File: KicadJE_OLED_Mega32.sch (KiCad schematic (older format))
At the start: 86 parts, among them J205 OUT1, J206 OUT2, J207 IN1, J208 IN2, J209 CV1, J210 CV2, SW201 Rotary_Encoder_Switch, SW202 Rotary_Encoder_Switch, U201 TL072

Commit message: Most components placed
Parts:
- removed C216, C217: 100n, AJ:C_0805_AJ, symbol Device:C
- gave numbers to parts that had none: 12
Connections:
- net 27_A3: no longer C219.1, R234.1
- net 28_A4: no longer C212.1, R230.2, SW202.A
- net 29_A5: no longer C210.1, R226.1, SW202.B
- new net 10_INT0: C212.1, R230.2, SW202.A
- new net 11_INT1: C210.1, R226.1, SW202.B
- new net D1: C219.1, R234.1
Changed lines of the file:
@@
 $EndDescr
 $Comp
-L Eurorack:Doepfer_Power_16pin P?
+L Eurorack:Doepfer_Power_16pin P201
 U 1 1 5CCBA3BD
 P 8650 1275
-F 0 "P?" H 9200 775 50  0000 C CNN
+F 0 "P201" H 9200 775 50  0000 C CNN
 F 1 "Doepfer_Power_16pin" H 8775 1825 50  0000 C CNN
 F 2 "Connector_IDC:IDC-Header_2x08_P2.54mm_Vertical" H 8650 1275 50  0001 C CNN
@@
 $EndComp
 $Comp
-L power:-12V #PWR?
+L power:-12V #PWR0112
 U 1 1 5CCD339B
 P 9350 1575
-F 0 "#PWR?" H 9350 1675 50  0001 C CNN
+F 0 "#PWR0112" H 9350 1675 50  0001 C CNN
 F 1 "-12V" V 9365 1703 50  0000 L CNN
 F 2 "" H 9350 1575 50  0001 C CNN
@@
 29_A5
 $Comp
-L power:+5V #PWR?
+L power:+5V #PWR0113
 U 1 1 6095FB46
 P 9975 875
-F 0 "#PWR?" H 9975 725 50  0001 C CNN
+F 0 "#PWR0113" H 9975 725 50  0001 C CNN
 F 1 "+5V" H 9990 1048 50  0000 C CNN
 F 2 "" H 9975 875 50  0001 C CNN
@@
 $EndComp
 $Comp
-L power:GND #PWR?
+L power:GND #PWR0114
 U 1 1 60960991
 P 9150 1375
-F 0 "#PWR?" H 9150 1125 50  0001 C CNN
+F 0 "#PWR0114" H 9150 1125 50  0001 C CNN
 F 1 "GND" H 9225 1375 50  0000 C CNN
 F 2 "" H 9150 1375 50  0001 C CNN
@@
 $EndComp
 $Comp
-L power:GND #PWR?
+L power:GND #PWR0115
 U 1 1 60960F4E
 P 8150 1375
-F 0 "#PWR?" H 8150 1125 50  0001 C CNN
+F 0 "#PWR0115" H 8150 1125 50  0001 C CNN
 F 1 "GND" H 8155 1202 50  0000 C CNN
 F 2 "" H 8150 1375 50  0001 C CNN
@@
 	9000 1175 9050 1175
 $Comp
-L power:+5V #PWR?
+L power:+5V #PWR0116
 U 1 1 6097BBB3
 P 3650 4250
-F 0 "#PWR?" H 3650 4100 50  0001 C CNN
+F 0 "#PWR0116" H 3650 4100 50  0001 C CNN
 F 1 "+5V" H 3665 4423 50  0000 C CNN
 F 2 "" H 3650 4250 50  0001 C CNN
@@
 $EndComp
 $Comp
-L power:+5V #PWR?
+L power:+5V #PWR0117
 U 1 1 6097C13F
 P 3650 5150
-F 0 "#PWR?" H 3650 5000 50  0001 C CNN
+F 0 "#PWR0117" H 3650 5000 50  0001 C CNN
 F 1 "+5V" H 3665 5323 50  0000 C CNN
 F 2 "" H 3650 5150 50  0001 C CNN
@@
 $EndComp
 $Comp
-L power:+5V #PWR?
+L power:+5V #PWR0118
 U 1 1 6097C5E9
 P 3650 6075
-F 0 "#PWR?" H 3650 5925 50  0001 C CNN
+F 0 "#PWR0118" H 3650 5925 50  0001 C CNN
 F 1 "+5V" H 3665 6248 50  0000 C CNN
 F 2 "" H 3650 6075 50  0001 C CNN
@@
 $EndComp
 $Comp
-L power:+5V #PWR?
+L power:+5V #PWR0119
 U 1 1 6097CB1B
 P 3650 6950
-F 0 "#PWR?" H 3650 6800 50  0001 C CNN
+F 0 "#PWR0119" H 3650 6800 50  0001 C CNN
 F 1 "+5V" H 3665 7123 50  0000 C CNN
 F 2 "" H 3650 6950 50  0001 C CNN
@@
 Wire Wire Line
 	2425 1100 2350 1100
-$Comp
-L Device:C C?
-U 1 1 60ACB69E
-P 10375 1025
-AR Path="/60ACB69E" Ref="C?"  Part="1"
-AR Path="/5CD3F059/60ACB69E" Ref="C?"  Part="1"
-AR Path="/608CA457/5CD3F059/60ACB69E" Ref="C?"  Part="1"
-AR Path="/608CA457/60ACB69E" Ref="C217"  Part="1"
-F 0 "C217" H 10250 1150 50  0000 L CNN
-F 1 "100n" H 10275 950 50  0000 L CNN
-F 2 "AJ:C_0805_AJ" H 10413 875 50  0001 C CNN
-F 3 "~" H 10375 1025 50  0001 C CNN
-	1    10375 1025
-	-1   0    0    1
-$EndComp
 $Comp
 L Device:C C?
@@
 $Comp
 L Device:C C?
-U 1 1 60ACB6AB
-P 10300 1650
-AR Path="/60ACB6AB" Ref="C?"  Part="1"
-AR Path="/5CD3F059/60ACB6AB" Ref="C?"  Part="1"
-AR Path="/608CA457/5CD3F059/60ACB6AB" Ref="C?"  Part="1"
-AR Path="/608CA457/60ACB6AB" Ref="C216"  Part="1"
-F 0 "C216" H 10175 1775 50  0000 L CNN
-F 1 "100n" H 10200 1575 50  0000 L CNN
-F 2 "AJ:C_0805_AJ" H 10338 1500 50  0001 C CNN
-F 3 "~" H 10300 1650 50  0001 C CNN
-	1    10300 1650
-	-1   0    0    1
-$EndComp
-$Comp
-L Device:C C?
 U 1 1 60ACB6B1
 P 10075 1650
@@
 	1    0    0    -1
 $EndComp
-Connection ~ 10300 1500
 $Comp
 L power:GND #PWR0240
@@
 $EndComp
 $Comp
-L Device:LED D?
+L Device:LED D209
 U 1 1 60B00B05
 P 9925 1800
-F 0 "D?" H 9900 1700 50  0000 C CNN
+F 0 "D209" H 9900 1700 50  0000 C CNN
 F 1 "LED" H 9800 1900 50  0000 C CNN
 F 2 "AJ:D_0805_AJ" H 9925 1800 50  0001 C CNN
@@
 	9775 1500 9775 1800
 $Comp
-L power:+5V #PWR?
+L power:+5V #PWR0120
 U 1 1 60B1856E
 P 4675 3025
-F 0 "#PWR?" H 4675 2875 50  0001 C CNN
+F 0 "#PWR0120" H 4675 2875 50  0001 C CNN
 F 1 "+5V" H 4690 3198 50  0000 C CNN
 F 2 "" H 4675 3025 50  0001 C CNN
@@
 	10150 875  10375 875
 $Comp
-L power:+12V #PWR?
+L power:+12V #PWR0121
 U 1 1 60B94BD0
 P 10375 875
-F 0 "#PWR?" H 10375 725 50  0001 C CNN
+F 0 "#PWR0121" H 10375 725 50  0001 C CNN
 F 1 "+12V" H 10390 1048 50  0000 C CNN
 F 2 "" H 10375 875 50  0001 C CNN
@@
 	1    0    0    -1
 $EndComp
-Connection ~ 10375 875
-$Comp
-L power:+12V #PWR?
+$Comp
+L power:+12V #PWR0122
 U 1 1 60B95768
 P 9525 1175
-F 0 "#PWR?" H 9525 1025 50  0001 C CNN
+F 0 "#PWR0122" H 9525 1025 50  0001 C CNN
 F 1 "+12V" H 9540 1348 50  0000 C CNN
 F 2 "" H 9525 1175 50  0001 C CNN
@@
 $EndComp
 $Comp
-L power:+5V #PWR?
+L power:+5V #PWR0123
 U 1 1 60B96020
 P 9425 1075
-F 0 "#PWR?" H 9425 925 50  0001 C CNN
+F 0 "#PWR0123" H 9425 925 50  0001 C CNN
 F 1 "+5V" H 9440 1248 50  0000 C CNN
 F 2 "" H 9425 1075 50  0001 C CNN
@@
 Connection ~ 9050 1175
 $Comp
-L power:GND #PWR?
+L power:GND #PWR0124
 U 1 1 60BE9216
 P 4550 3275
-F 0 "#PWR?" H 4550 3025 50  0001 C CNN
+F 0 "#PWR0124" H 4550 3025 50  0001 C CNN
 F 1 "GND" H 4555 3102 50  0000 C CNN
 F 2 "" H 4550 3275 50  0001 C CNN
@@
 	4425 3275 4550 3275
 $Comp
-L Connector:Conn_01x04_Female J?
+L Connector:Conn_01x04_Female J201
 U 1 1 60BF44F5
 P 975 2100
-F 0 "J?" H 867 1675 50  0000 C CNN
+F 0 "J201" H 867 1675 50  0000 C CNN
 F 1 "OLED" H 867 1766 50  0000 C CNN
 F 2 "Connector_PinSocket_2.54mm:PinSocket_1x04_P2.54mm_Vertical" H 975 2100 50  0001 C CNN
@@
 $EndComp
 $Comp
-L power:+5V #PWR?
+L power:+5V #PWR0125
 U 1 1 60C0BC24
 P 1725 1750
-F 0 "#PWR?" H 1725 1600 50  0001 C CNN
+F 0 "#PWR0125" H 1725 1600 50  0001 C CNN
 F 1 "+5V" H 1740 1923 50  0000 C CNN
 F 2 "" H 1725 1750 50  0001 C CNN
@@
 $EndComp
 $Comp
-L Device:Jumper_NC_Dual JP?
+L Device:Jumper_NC_Dual JP201
 U 1 1 60CA048D
 P 1275 2200
-F 0 "JP?" V 1575 2125 50  0000 L CNN
+F 0 "JP201" V 1575 2125 50  0000 L CNN
 F 1 "1" H 1320 2302 50  0000 L CNN
 F 2 "Jumper:SolderJumper-3_P1.3mm_Bridged12_Pad1.0x1.5mm_NumberLabels" H 1275 2200 50  0001 C CNN
@@
 	1175 2100 1425 2100
 $Comp
-L Device:Jumper_NC_Dual JP?
+L Device:Jumper_NC_Dual JP202
 U 1 1 60CD1C03
 P 1525 2100
-F 0 "JP?" V 1925 2050 50  0000 L CNN
+F 0 "JP202" V 1925 2050 50  0000 L CNN
 F 1 "2" H 1570 2202 50  0000 L CNN
 F 2 "Jumper:SolderJumper-3_P1.3mm_Bridged12_Pad1.0x1.5mm_NumberLabels" H 1525 2100 50  0001 C CNN
@@
 $EndComp
 $Comp
-L Device:Jumper_NC_Dual JP?
+L Device:Jumper_NC_Dual JP203
 U 1 1 60CD20EB
 P 1725 2000
-F 0 "JP?" V 2075 1925 50  0000 L CNN
+F 0 "JP203" V 2075 1925 50  0000 L CNN
 F 1 "3" V 1770 2102 50  0000 L CNN
 F 2 "Jumper:SolderJumper-3_P1.3mm_Bridged12_Pad1.0x1.5mm_NumberLabels" H 1725 2000 50  0001 C CNN
@@
 	1175 1900 1800 1900
 $Comp
-L Device:Jumper_NC_Dual JP?
+L Device:Jumper_NC_Dual JP204
 U 1 1 60CD252A
 P 1900 1900
-F 0 "JP?" V 2300 1850 50  0000 L CNN
+F 0 "JP204" V 2300 1850 50  0000 L CNN
 F 1 "4" H 1945 2002 50  0000 L CNN
 F 2 "Jumper:SolderJumper-3_P1.3mm_Bridged12_Pad1.0x1.5mm_NumberLabels" H 1900 1900 50  0001 C CNN
@@
 $EndComp
 $Comp
-L power:+5V #PWR?
+L power:+5V #PWR0126
 U 1 1 60CF91B4
 P 1425 2450
-F 0 "#PWR?" H 1425 2300 50  0001 C CNN
+F 0 "#PWR0126" H 1425 2300 50  0001 C CNN
 F 1 "+5V" H 1440 2623 50  0000 C CNN
 F 2 "" H 1425 2450 50  0001 C CNN
@@
 	4950 2625 4425 2625
 $Comp
-L Connector:Conn_01x06_Female J?
+L Connector:Conn_01x06_Female J211
 U 1 1 60DAC92E
 P 2150 3050
-F 0 "J?" V 1996 3298 50  0000 L CNN
+F 0 "J211" V 1996 3298 50  0000 L CNN
 F 1 "FrontLED" V 2087 3298 50  0000 L CNN
 F 2 "Connector_PinSocket_2.54mm:PinSocket_1x06_P2.54mm_Vertical" H 2150 3050 50  0001 C CNN
@@
 Connection ~ 10875 1775
 $Comp
-L power:+12V #PWR?
+L power:+12V #PWR0127
 U 1 1 60E752FF
 P 10875 975
-F 0 "#PWR?" H 10875 825 50  0001 C CNN
+F 0 "#PWR0127" H 10875 825 50  0001 C CNN
 F 1 "+12V" V 10890 1103 50  0000 L CNN
 F 2 "" H 10875 975 50  0001 C CNN
@@
 Connection ~ 1450 6950
 $Comp
-L Connector:Conn_01x03_Female J?
+L Connector:Conn_01x03_Female J202
 U 1 1 610AFCC8
 P 1000 1250
-F 0 "J?" H 892 925 50  0000 C CNN
+F 0 "J202" H 892 925 50  0000 C CNN
 F 1 "ADC Input" H 892 1016 50  0000 C CNN
 F 2 "Connector_PinSocket_2.54mm:PinSocket_1x03_P2.54mm_Vertical" H 1000 1250 50  0001 C CNN
@@
 	3175 6375 3225 6375
 $Comp
-L Connector:Conn_01x02_Female J?
+L Connector:Conn_01x02_Female J204
 U 1 1 61168D11
 P 1100 4650
-F 0 "J?" H 992 4325 50  0000 C CNN
+F 0 "J204" H 992 4325 50  0000 C CNN
 F 1 "Out1" H 1200 4600 50  0000 C CNN
 F 2 "Connector_PinSocket_2.54mm:PinSocket_1x02_P2.54mm_Vertical" H 1100 4650 50  0001 C CNN
@@
 $EndComp
 $Comp
-L Connector:Conn_01x02_Female J?
+L Connector:Conn_01x02_Female J203
 U 1 1 6116995C
 P 1075 5150
-F 0 "J?" H 967 4825 50  0000 C CNN
+F 0 "J203" H 967 4825 50  0000 C CNN
 F 1 "Out2" H 1175 5100 50  0000 C CNN
 F 2 "Connector_PinSocket_2.54mm:PinSocket_1x02_P2.54mm_Vertical" H 1075 5150 50  0001 C CNN
@@
 Connection ~ 1450 4650
 $Comp
-L Connector:Conn_01x02_Female J?
+L Connector:Conn_01x02_Female J212
 U 1 1 611E2AB8
 P 9875 2300
-F 0 "J?" H 9767 1975 50  0000 C CNN
+F 0 "J212" H 9767 1975 50  0000 C CNN
 F 1 "-12V Front" H 9975 2250 50  0000 C CNN
 F 2 "Connector_PinSocket_2.54mm:PinSocket_1x02_P2.54mm_Vertical" H 9875 2300 50  0001 C CNN
@@
 30_A6
 Text GLabel 10750 4125 2    50   Input ~ 0
-27_A3
+D1
 Text GLabel 8525 4125 0    50   Input ~ 0
-28_A4
-Text GLabel 8525 4325 0    50   Input ~ 0
-29_A5
+10_INT0
 Text GLabel 1275 1150 2    50   Input ~ 0
 30_A6
@@
 	9350 3925 9275 3925
 Connection ~ 9275 3925
+Text GLabel 8525 4325 0    50   Input ~ 0
+11_INT1
+Text GLabel 4425 2225 2    50   Input ~ 0
+10_INT0
+Text GLabel 4425 2325 2    50   Input ~ 0
+11_INT1
+Text GLabel 4425 1075 2    50   Input ~ 0
+D1
 $EndSCHEMATC

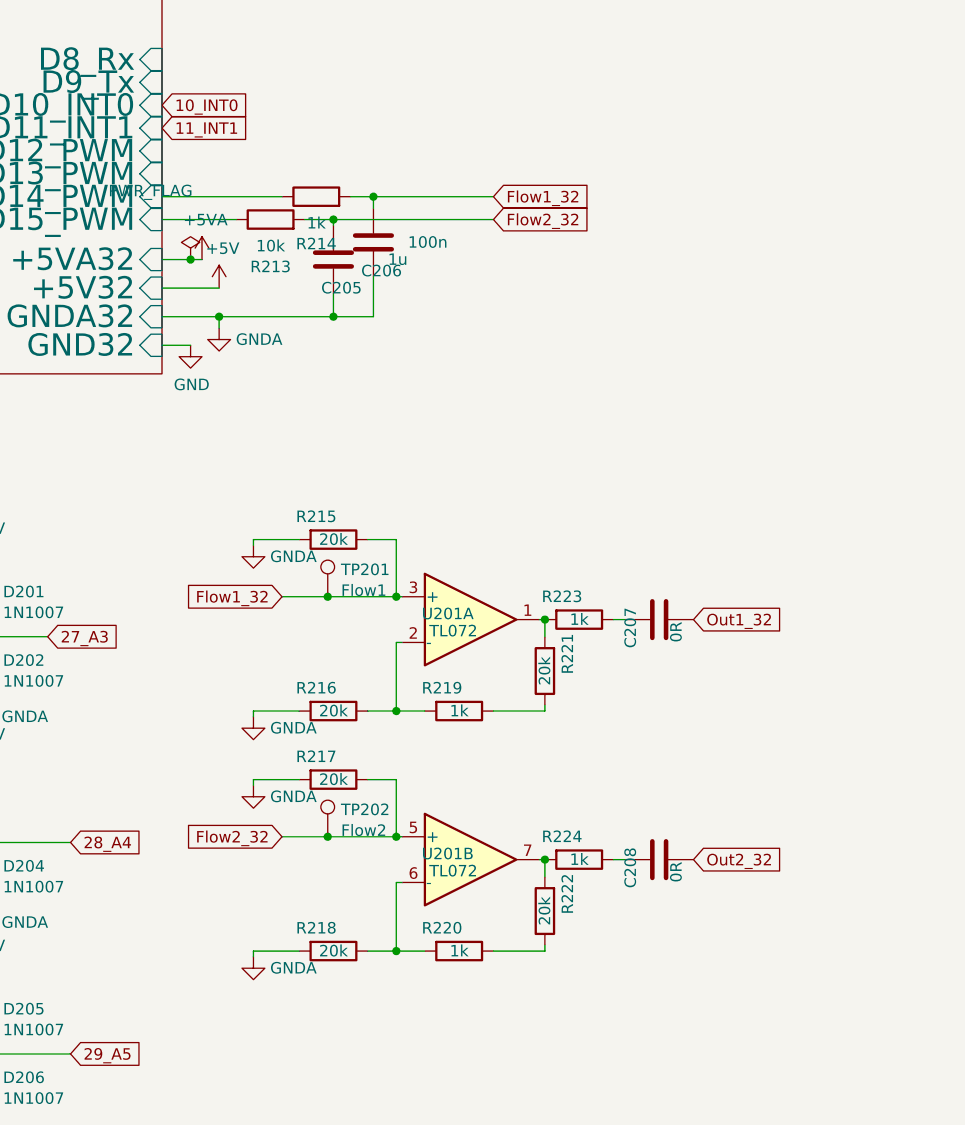
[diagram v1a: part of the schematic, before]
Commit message: Sallen Key LP filter added to output
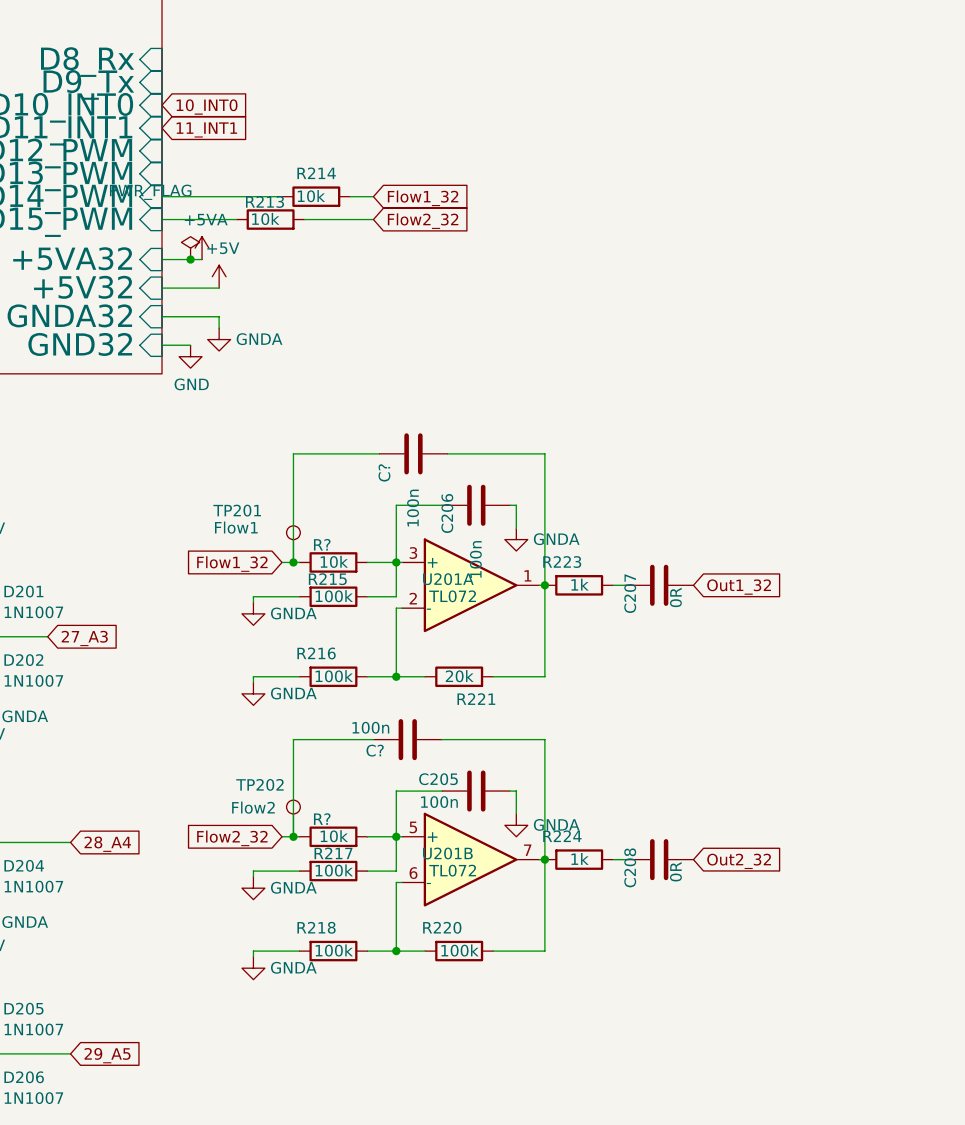
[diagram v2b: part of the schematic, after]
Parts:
- removed R219: 1k, AJ:R_0805_AJ, symbol Device:R
- removed R222: 20k, AJ:R_0805_AJ, symbol Device:R
- added C?: 100n, AJ:C_0805_AJ, symbol Device:C
- added C?: 100n, Capacitor_SMD:C_1206_3216Metric, symbol Device:C
- added R? (x2): 10k, AJ:R_0805_AJ, symbol Device:R
- C205: value 1u -> 100n; footprint Capacitor_SMD:C_1206_3216Metric -> AJ:C_0805_AJ
- C206: footprint Capacitor_SMD:C_1206_3216Metric -> AJ:C_0805_AJ
- R214: value 1k -> 10k
- R215, R216, R217, R218: value 20k -> 100k
- R220: value 1k -> 100k
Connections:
- net Flow1_32: now also C?.1, R?.1; no longer C206.2, R215.1, U201.3 (+)
- net Flow2_32: now also C?.1, R?.1; no longer C205.2, R217.1, U201.5 (+)
- net GNDA: now also C205.2, C206.2; no longer C205.1, C206.1
- net at R221.2, R223.2, U201.1: now also C?.2
- net at R216.1, U201.2 (-): now also R221.1
- net at R224.2, U201.7: now also R220.1, C?.2
- new net: C206.1, R215.1, R?.2, U201.3 (+)
- new net: C205.1, R217.1, R?.2, U201.5 (+)
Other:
- moved on the sheet: C205, C206, C207, R215, R216, R217, R221, R223, TP201, TP202, U201A

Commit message: 6pin input hdr
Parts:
- C216: renamed from C?; footprint Capacitor_SMD:C_1206_3216Metric -> AJ:C_0805_AJ
- J202: footprint Connector_PinSocket_2.54mm:PinSocket_1x03_P2.54mm_Vertical -> Connector_PinSocket_2.54mm:PinSocket_2x03_P2.54mm_Vertical; symbol Connector:Conn_01x03_Female -> Connector:Conn_01x06_Female
- R221: value 20k -> 100k
- gave numbers to parts that had none: 3
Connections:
- net ATMega32A.sch/D14_PWM is gone; now on net Flow1_32: R214.1
- net ATMega32A.sch/D15_PWM is gone; now on net Flow2_32: R213.1
- net 27_A3: now also J202.6 (Pin_6)
- net 28_A4: now also J202.5 (Pin_5)
- net 29_A5: now also J202.4 (Pin_4)
- net Flow1_32: no longer C217.1, R214.2, R219.1, TP201.1
- net Flow2_32: no longer C216.1, R213.2, R222.1, TP202.1
- new net: C217.1, R214.2, R219.1, TP201.1
- new net: C216.1, R213.2, R222.1, TP202.1
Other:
- moved on the sheet: C205, C206, C207, C208, C209, C210, C211, C212, C213, C214, C215, C216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
